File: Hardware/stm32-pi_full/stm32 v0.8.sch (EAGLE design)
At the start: 259 parts, among them J1 SOLDERJUMPERNO, Q1 MMBT3906, Q2 MMBT3904, Q3 MMBT3904, U1 ESP32-WROOM-32D

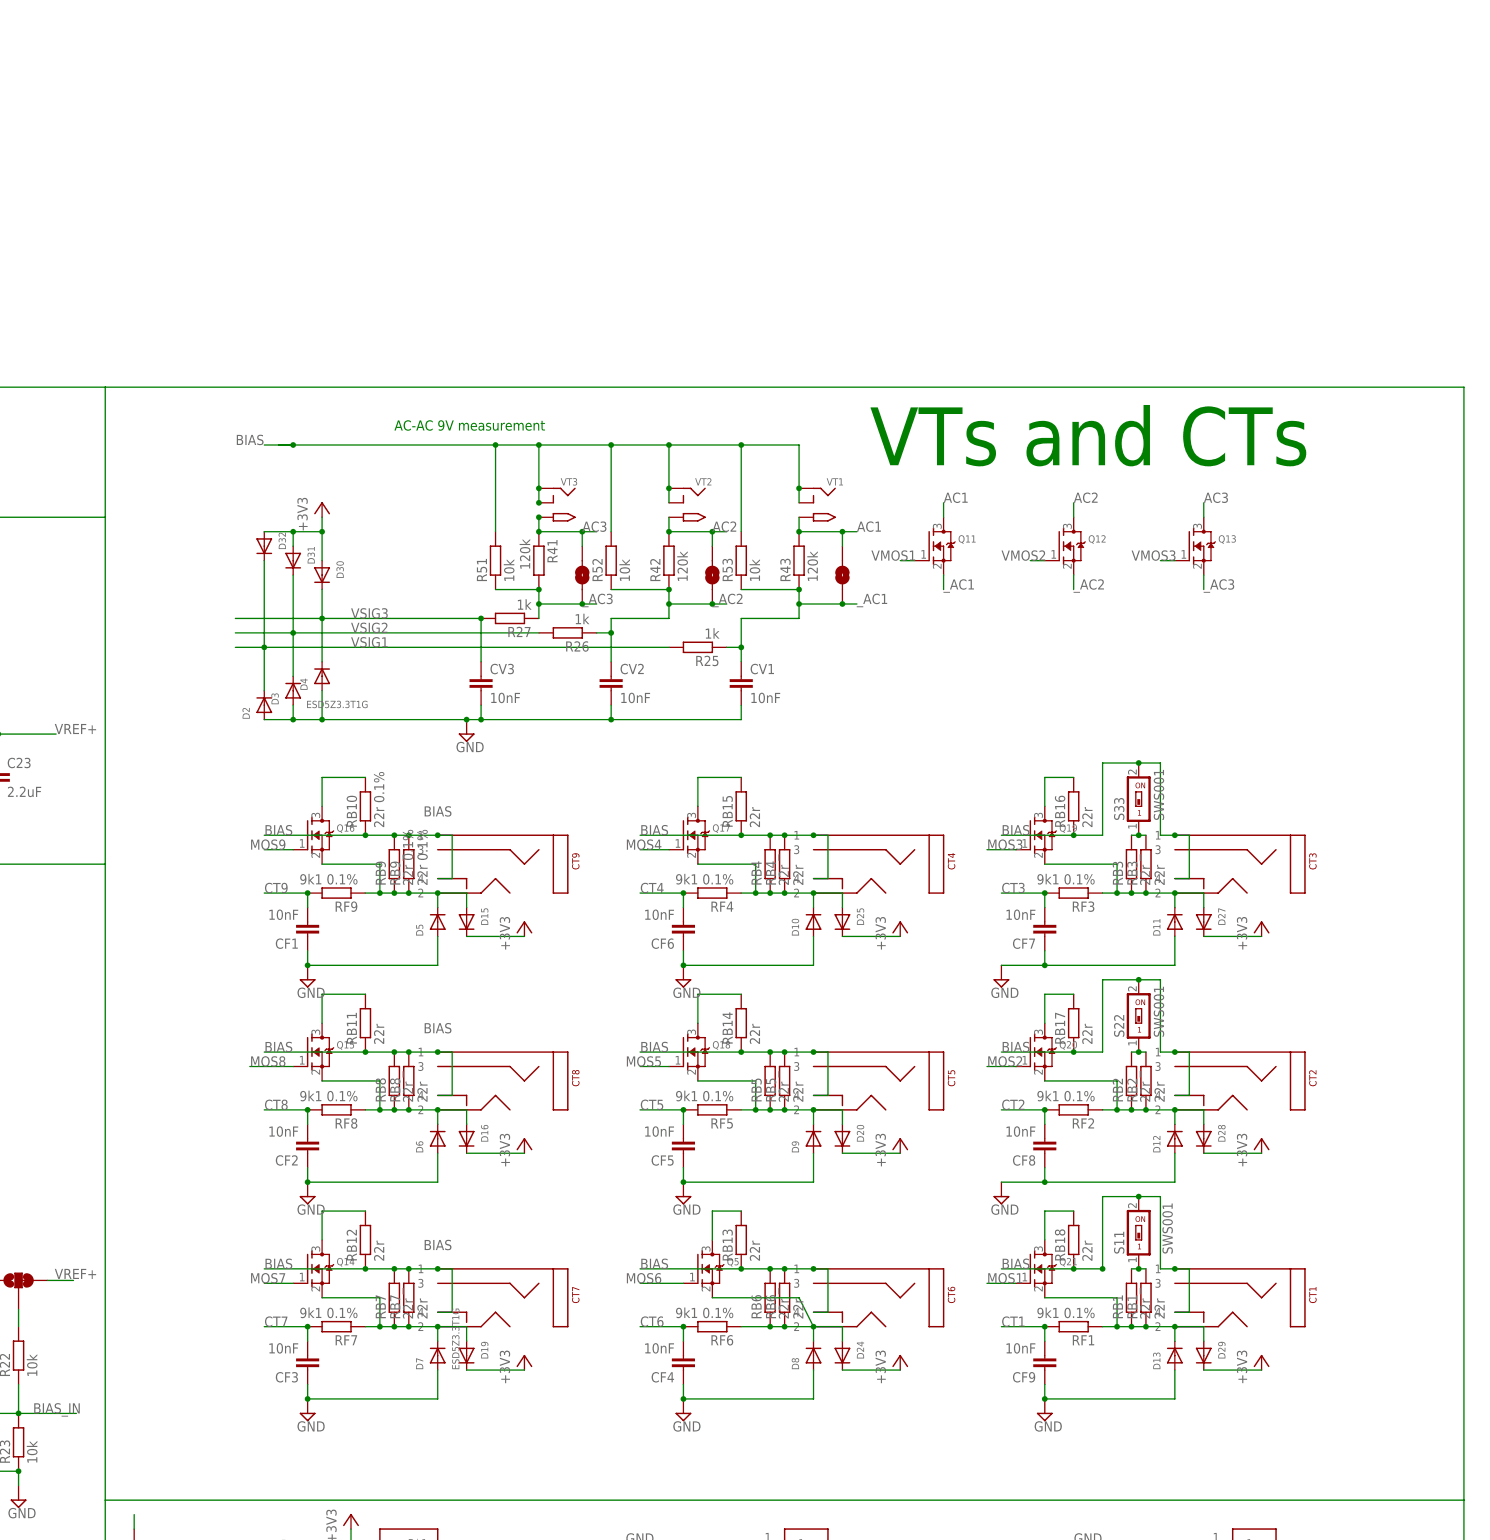
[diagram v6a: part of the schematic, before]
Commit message: phase correction tested, seems to work!
buffer index shifting, maximum PF hunting, modal value
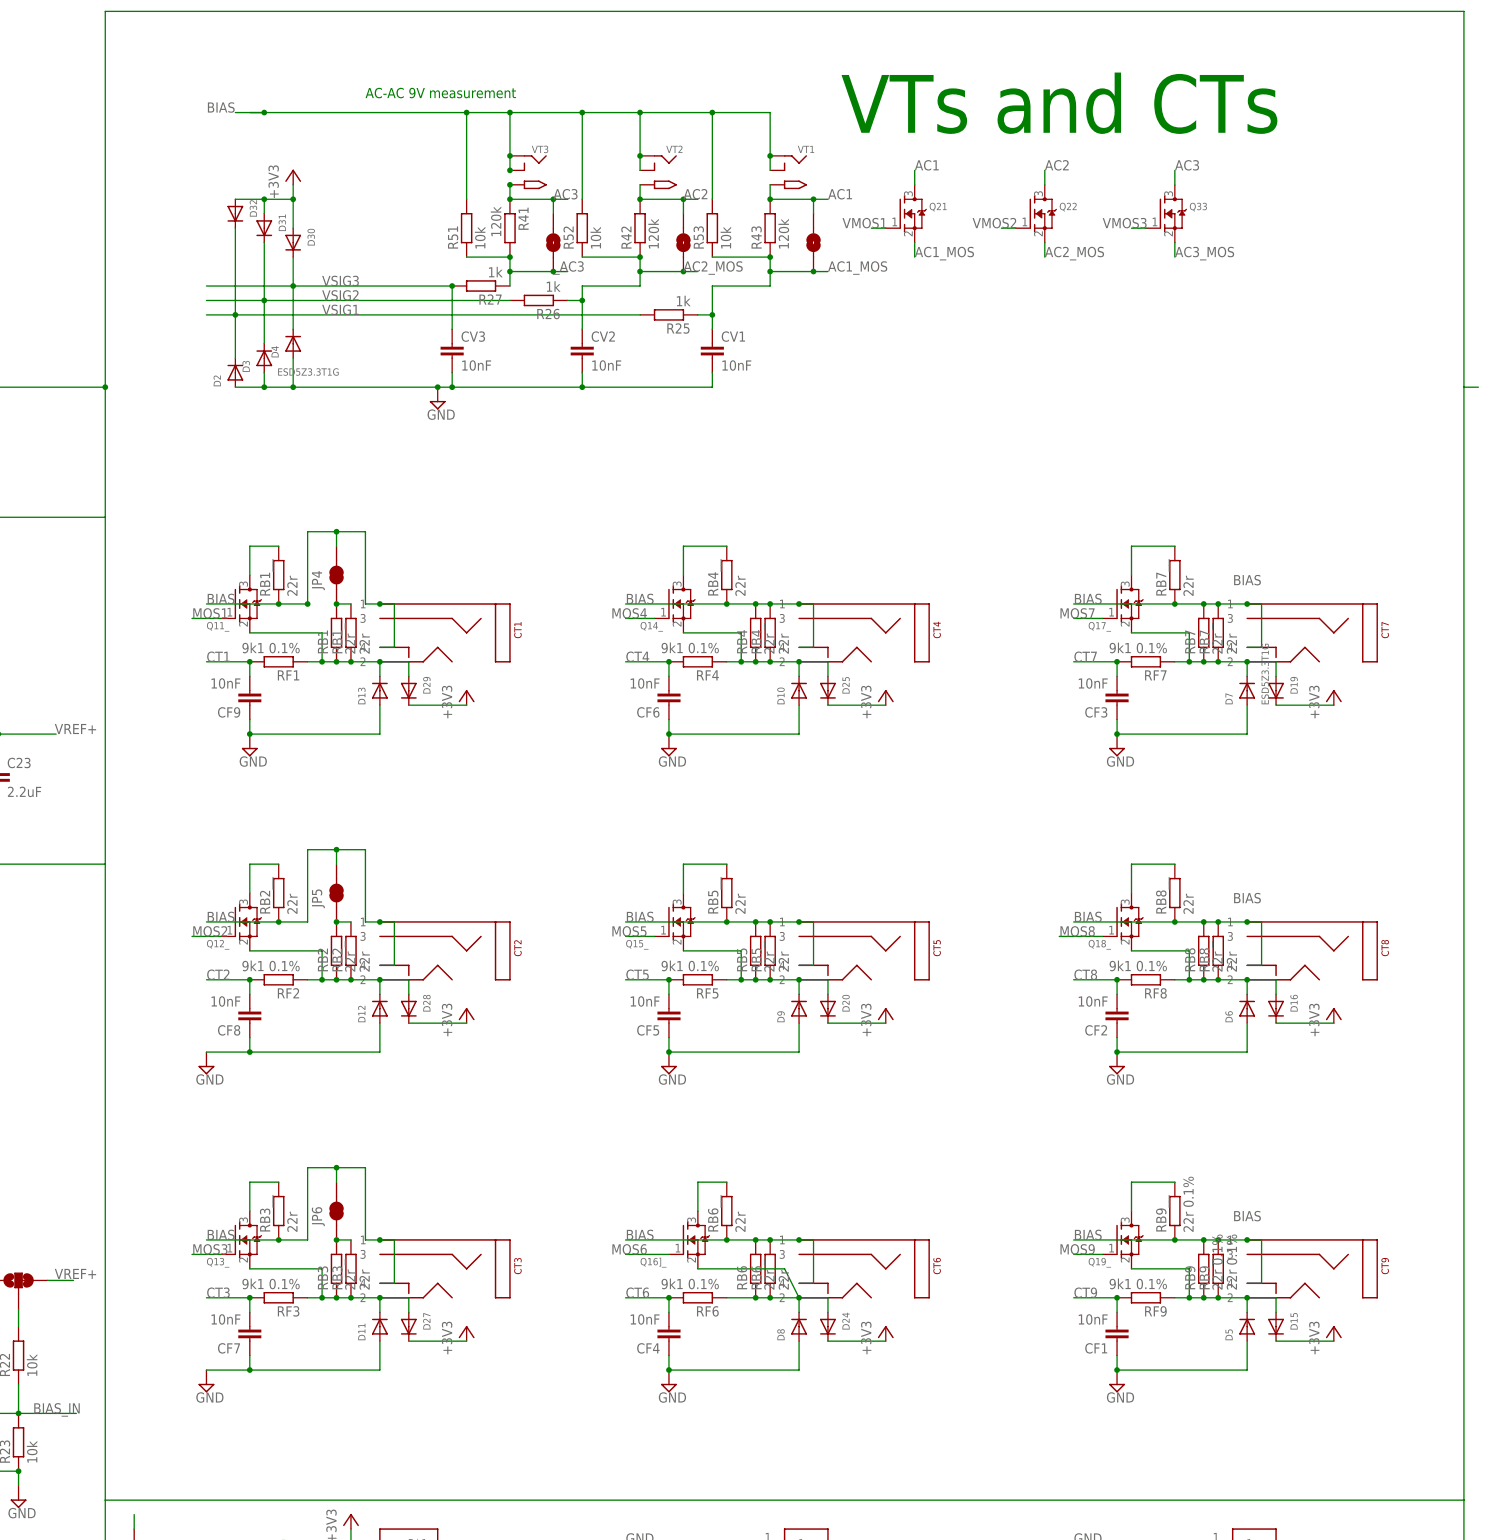
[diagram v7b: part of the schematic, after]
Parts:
- removed Q11, Q12, Q13, Q14, Q15, Q16, Q17, Q18, Q19, Q20, Q5: (no value), adafruit:MOSFET-NREFLOW
- removed RB10: 22r 0.1%, rcl:R-EU_R1210
- removed RB11, RB12, RB13, RB14, RB15, RB16, RB17, RB18: 22r, rcl:R-EU_R1210
- removed S11, S22, S33: SWS001, smd-special:SWS001
- added JP4, JP5, JP6: JUMPER-SMT_2_NC_TRACE_NO-SILK, SparkFun-Jumpers:JUMPER-SMT_2_NC_TRACE_NO-SILK
- added Q11_, Q12_, Q13_, Q14_, Q15_, Q16]_, Q17_, Q18_, Q19_, Q22, Q33: (no value), adafruit:MOSFET-NREFLOW
- added RB1__, RB2__, RB3__, RB4__, RB5__, RB6__, RB7__, RB8__: 22r, rcl:R-EU_R1210
- added RB9__: 22r 0.1%, rcl:R-EU_R1210
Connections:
- removed net _AC1: CV1.1, Q11.S, R25.1, R43.1, R53.1, SJ37.1
- removed net _AC2: CV2.1, Q12.S, R26.1, R42.1, R52.1, SJ36.1
- new net AC1_MOS: CV1.1, Q21.S, R25.1, R43.1, R53.1, SJ37.1
- new net AC2_MOS: CV2.1, Q22.S, R26.1, R42.1, R52.1, SJ36.1
- new net AC3_MOS: Q33.S
- net AC1: now also Q21.D; no longer Q11.D
- net AC2: now also Q22.D; no longer Q12.D
- net AC3: now also Q33.D; no longer Q13.D
- net BIAS: now also JP4.2, JP5.2, JP6.2, RB1__.1, RB2__.1, RB3__.1, RB4__.1, RB5__.1, RB6__.1, RB7__.1, RB8__.1, RB9__.1; no longer RB10.1, RB11.1, RB12.1, RB13.1, RB14.1, RB15.1, RB16.1, RB17.1, RB18.1, S11.2, S22.2, S33.2
- net CT_IN1: now also Q11_.S; no longer Q21.S
- net CT_IN2: now also Q12_.S; no longer Q20.S
- net CT_IN3: now also Q13_.S; no longer Q19.S
- net MOS0: now also Q11_.D, RB1__.2; no longer Q21.D, RB18.2
- net MOS1: now also Q11_.G, Q12_.D, RB2__.2; no longer Q20.D, Q21.G, RB17.2
- net MOS2: now also Q12_.G, Q13_.D, RB3__.2; no longer Q19.D, Q20.G, RB16.2
- net MOS3: now also Q13_.G; no longer Q19.G
- net MOS4: now also Q14_.G; no longer Q17.G
- net MOS5: now also Q15_.G; no longer Q18.G
- net MOS6: now also Q16]_.G; no longer Q5.G
- net MOS7: now also Q17_.G; no longer Q14.G
- net MOS8: now also Q18_.G; no longer Q15.G
- net MOS9: now also Q19_.G; no longer Q16.G
- net N$10: now also Q17_.S; no longer Q14.S
- net N$2: now also Q19_.S; no longer Q16.S
- net N$26: now also JP4.1; no longer S11.1
- net N$27: now also JP5.1; no longer S22.1
- net N$28: now also JP6.1; no longer S33.1
- net N$37: now also Q14_.D, RB4__.2; no longer Q17.D, RB15.2
- net N$38: now also Q16]_.S; no longer Q5.S
- net N$39: now also Q15_.S; no longer Q18.S
- net N$40: now also Q14_.S; no longer Q17.S
- net N$45: now also Q19_.D, RB9__.2; no longer Q16.D, RB10.2
- net N$46: now also Q18_.D, RB8__.2; no longer Q15.D, RB11.2
- net N$47: now also Q15_.D, RB5__.2; no longer Q18.D, RB14.2
- net N$48: now also Q16]_.D, RB6__.2; no longer Q5.D, RB13.2
- net N$49: now also Q17_.D, RB7__.2; no longer Q14.D, RB12.2
- net N$8: now also Q18_.S; no longer Q15.S
- net VMOS1: now also Q21.G; no longer Q11.G
- net VMOS2: now also Q22.G; no longer Q12.G
- net VMOS3: now also Q33.G; no longer Q13.G
- net _AC3: no longer Q13.S
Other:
- moved on the sheet: CF1, CF2, CF3, CF4, CF5, CF6, CF7, CF8, CF9, CT1, CT2, CT3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

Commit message: commit
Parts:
- removed C20: 100nF, resistor:C-EUC0603
- removed D21: ESD5Z3.3T1G, microbuilder:DIODESOD-523
- removed U$1, U$3: 3.5MM_TERMINAL_BLOCK, 3.5mm terminal block rs pro:3.5MM_TERMINAL_BLOCK
- removed VT2, VT3: ADC-028-2-T, adafruit:2.1MMJACKSMT
- added U$10: 3.5MM_TB_X6, 3.5mm terminal block rs pro:3.5MM_TB_X6
- added U$9: 3.5MM_TB_X4, 3.5mm terminal block rs pro:3.5MM_TB_X4
- RB1: value 22r -> 22r 0.3W 1%
- RB1_: value 22r -> 22r 0.5W
- U$4: value 3.5MM_TERMINAL_BLOCK -> 3.5MM_TB_X6; device 3.5mm terminal block rs pro:3.5MM_TERMINAL_BLOCK -> 3.5mm terminal block rs pro:3.5MM_TB_X6
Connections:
- net BIAS_ renamed BIAS*
- net +3V3: now also D30.C, D31.C, D32.C, U$10.P$5; no longer D30.A, D31.A, D32.A, U$1.P$3, U$3.P$3
- net AC1: now also U$10.P$2
- net AC2: now also U$10.P$3; no longer VT2.TIP
- net AC3: now also U$10.P$4; no longer VT3.TIP
- net BIAS: now also U$10.P$1; no longer VT2.RING, VT2.RING_SW, VT3.RING, VT3.RING_SW
- net GND: now also U$10.P$6, U$4.P$4, U$4.P$5; no longer C20.2, D21.A, U$1.P$1, U$3.P$1
- net PUSHIN_1: now also U$4.P$2; no longer U$1.P$2
- net PUSHIN_2: now also U$4.P$6; no longer U$3.P$2
- net PUSHIN_3: no longer C20.1, D21.C, U$4.P$2
- net VSIG1: now also D30.A; no longer D32.C
- net VSIG2: now also D31.A; no longer D31.C
- net VSIG3: now also D32.A; no longer D30.C
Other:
- note added: "Reference"
- note removed: "Voltage Reference"
- moved on the sheet: D30, D31, D32
